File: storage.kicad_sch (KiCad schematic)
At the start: 5 parts, among them J14 DM3CS-SF, U7 MX25V4006EM1I-13G

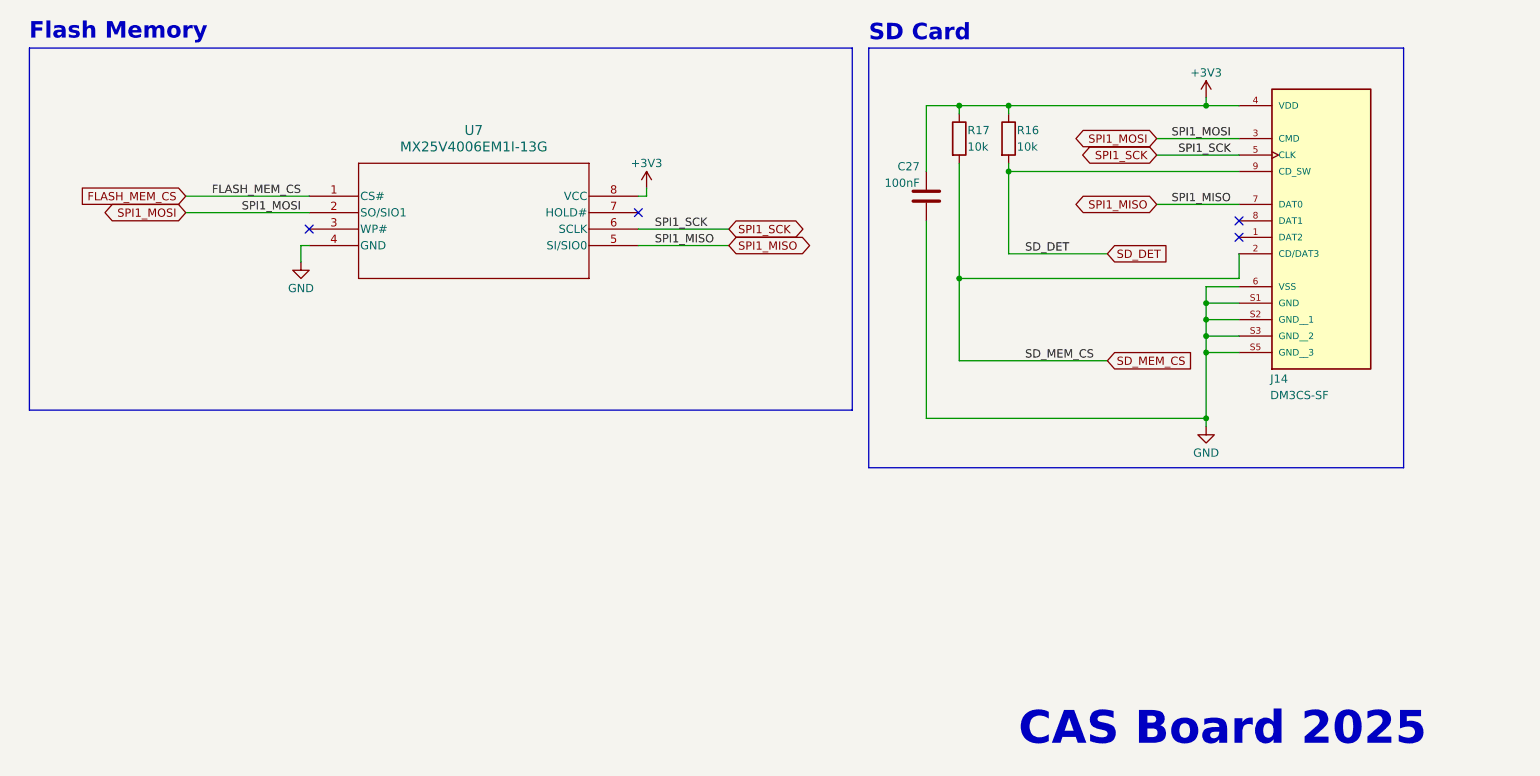
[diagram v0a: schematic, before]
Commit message: Use heirarchical labels
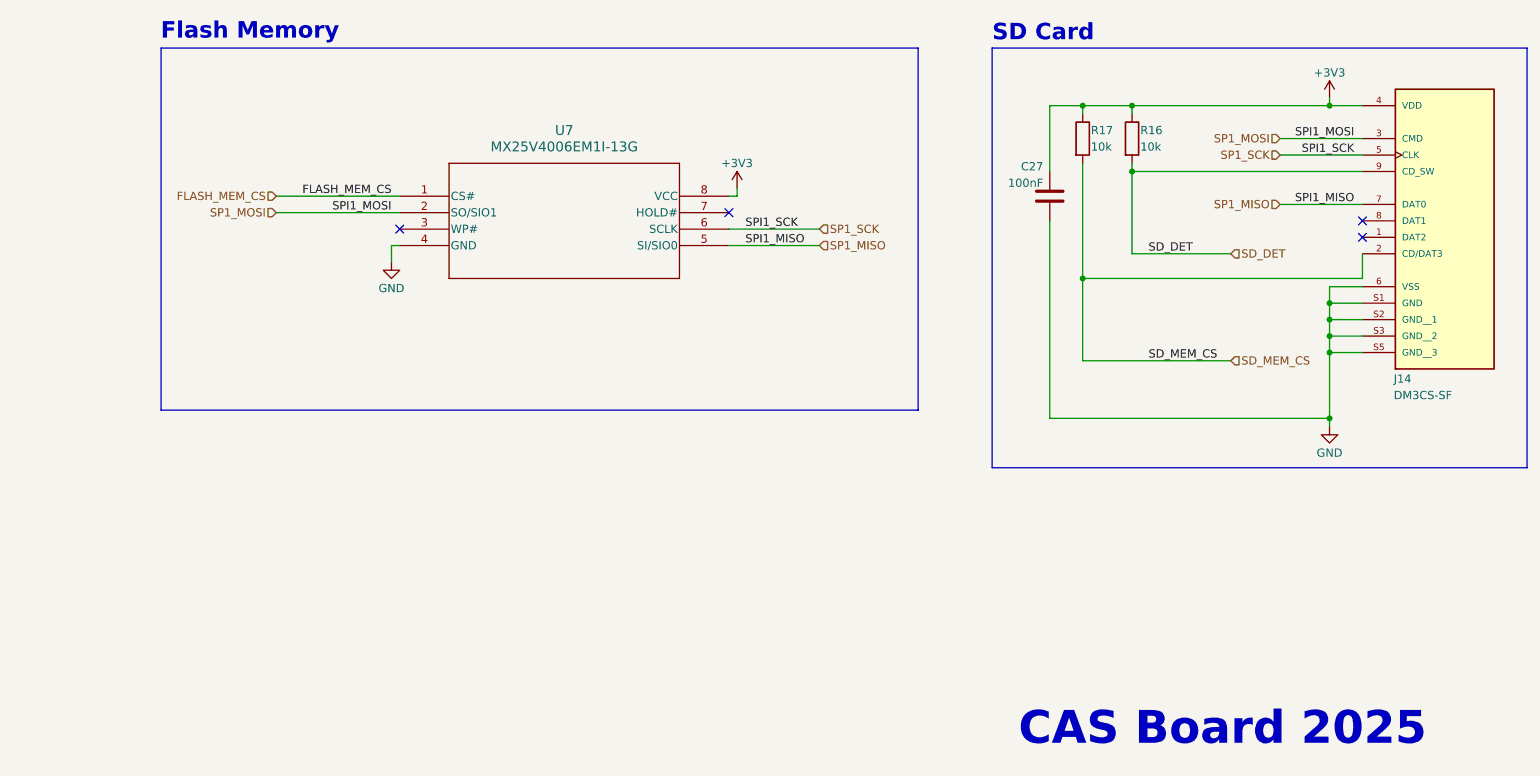
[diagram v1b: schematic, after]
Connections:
- net SPI1_MISO renamed SP1_MISO
- net SPI1_MOSI renamed SP1_MOSI
- net SPI1_SCK renamed SP1_SCK
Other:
- moved on the sheet: C27, J14, R16, R17, U7

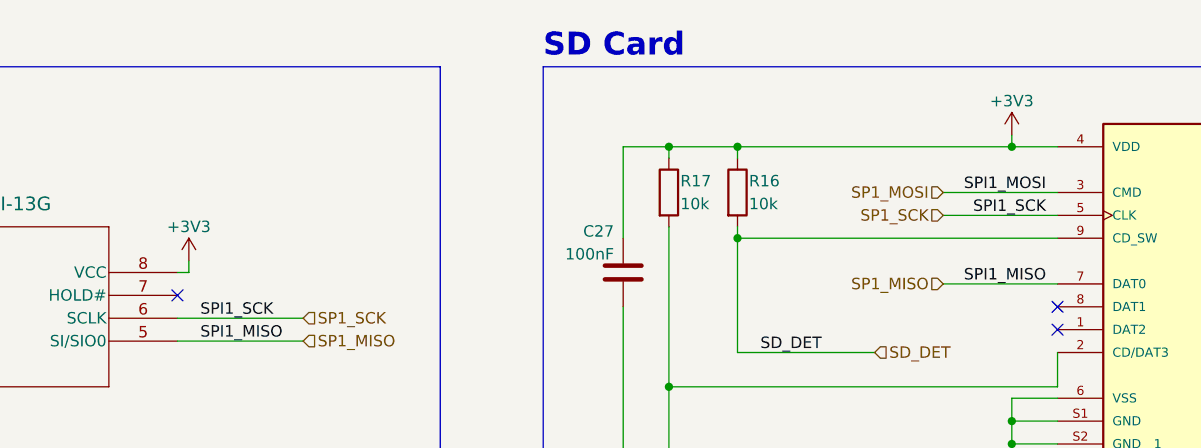
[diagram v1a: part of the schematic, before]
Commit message: Initial layout for PCB components, updated README with images. Removed some test points and headers from final layout. Pending addition of buzzer. Pending additional power testing and pending routing.
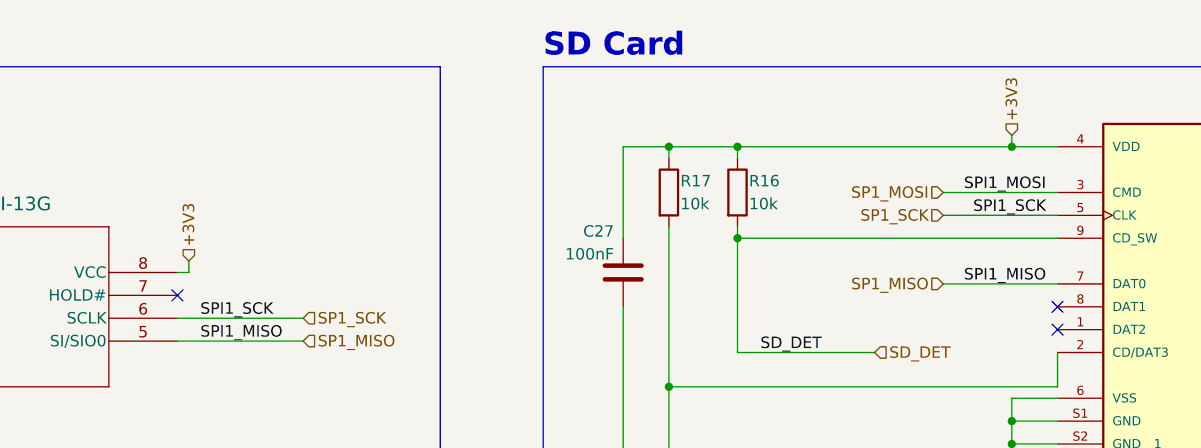
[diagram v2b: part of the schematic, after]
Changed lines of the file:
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@@
+		)
+	)
+	(hierarchical_label "+3V3"
+		(shape input)
+		(at 226.06 76.2 90)
+		(effects
+			(font
+				(size 1.27 1.27)
+			)
+			(justify left)
 		)
 	)
@@
 			)
 			(justify right)
+		)
+	)
+	(hierarchical_label "+3V3"
+		(shape input)
+		(at 134.62 90.17 90)
+		(effects
+			(font
+				(size 1.27 1.27)
+			)
+			(justify left)
 		)
 	)
@@
 	)
 	(symbol
-		(lib_id "power:+3V3")
-		(at 134.62 90.17 0)
-		(unit 1)
-		(exclude_from_sim no)
-		(in_bom yes)
-		(on_board yes)
-		(dnp no)
-		(property "Reference" "#PWR042"
-			(at 134.62 93.98 0)
-			(effects
-				(font
-					(size 1.27 1.27)
-				)
-				(hide yes)
-			)
-		)
-		(property "Value" "+3V3"
-			(at 134.62 86.36 0)
-			(effects
-				(font
-					(size 1.27 1.27)
-				)
-			)
-		)
-		(property "Footprint" ""
-			(at 134.62 90.17 0)
-			(effects
-				(font
-					(size 1.27 1.27)
-				)
-				(hide yes)
-			)
-		)
-		(property "Datasheet" ""
-			(at 134.62 90.17 0)
-			(effects
-				(font
-					(size 1.27 1.27)
-				)
-				(hide yes)
-			)
-		)
-		(property "Description" "Power symbol creates a global label with name \"+3V3\""
-			(at 134.62 90.17 0)
-			(effects
-				(font
-					(size 1.27 1.27)
-				)
-				(hide yes)
-			)
-		)
-		(pin "1"
-		)
-		(instances
-			(project "SimplerFlight_v2"
-				(path "/05521696-5bcb-4d0e-9e87-bbc993e58ce4/5650f10d-f3d9-4005-a2cb-b3a110a98d48"
-					(reference "#PWR042")
-					(unit 1)
-				)
-			)
-		)
-	)
-	(symbol
 		(lib_id "power:GND")
 		(at 81.28 101.6 0)
@@
 					(unit 1)
 				)
-			)
-		)
-	)
-	(symbol
-		(lib_id "power:+3V3")
-		(at 226.06 76.2 0)
-		(unit 1)
-		(exclude_from_sim no)
-		(in_bom yes)
-		(on_board yes)
-		(dnp no)
-		(property "Reference" "#PWR032"
-			(at 226.06 80.01 0)
-			(effects
-				(font
-					(size 1.27 1.27)
-				)
-				(hide yes)
-			)
-		)
-		(property "Value" "+3V3"
-			(at 226.06 72.39 0)
-			(effects
-				(font
-					(size 1.27 1.27)
-				)
-			)
-		)
-		(property "Footprint" ""
-			(at 226.06 76.2 0)
-			(effects
-				(font
-					(size 1.27 1.27)
-				)
-				(hide yes)
-			)
-		)
-		(property "Datasheet" ""
-			(at 226.06 76.2 0)
-			(effects
-				(font
-					(size 1.27 1.27)
-				)
-				(hide yes)
-			)
-		)
-		(property "Description" "Power symbol creates a global label with name \"+3V3\""
-			(at 226.06 76.2 0)
-			(effects
-				(font
-					(size 1.27 1.27)
-				)
-				(hide yes)
-			)
-		)
-		(pin "1"
-		)
-		(instances
-			(project "SimplerFlight_v2"
-				(path "/05521696-5bcb-4d0e-9e87-bbc993e58ce4/5650f10d-f3d9-4005-a2cb-b3a110a98d48"
-					(reference "#PWR032")
-					(unit 1)
-				)

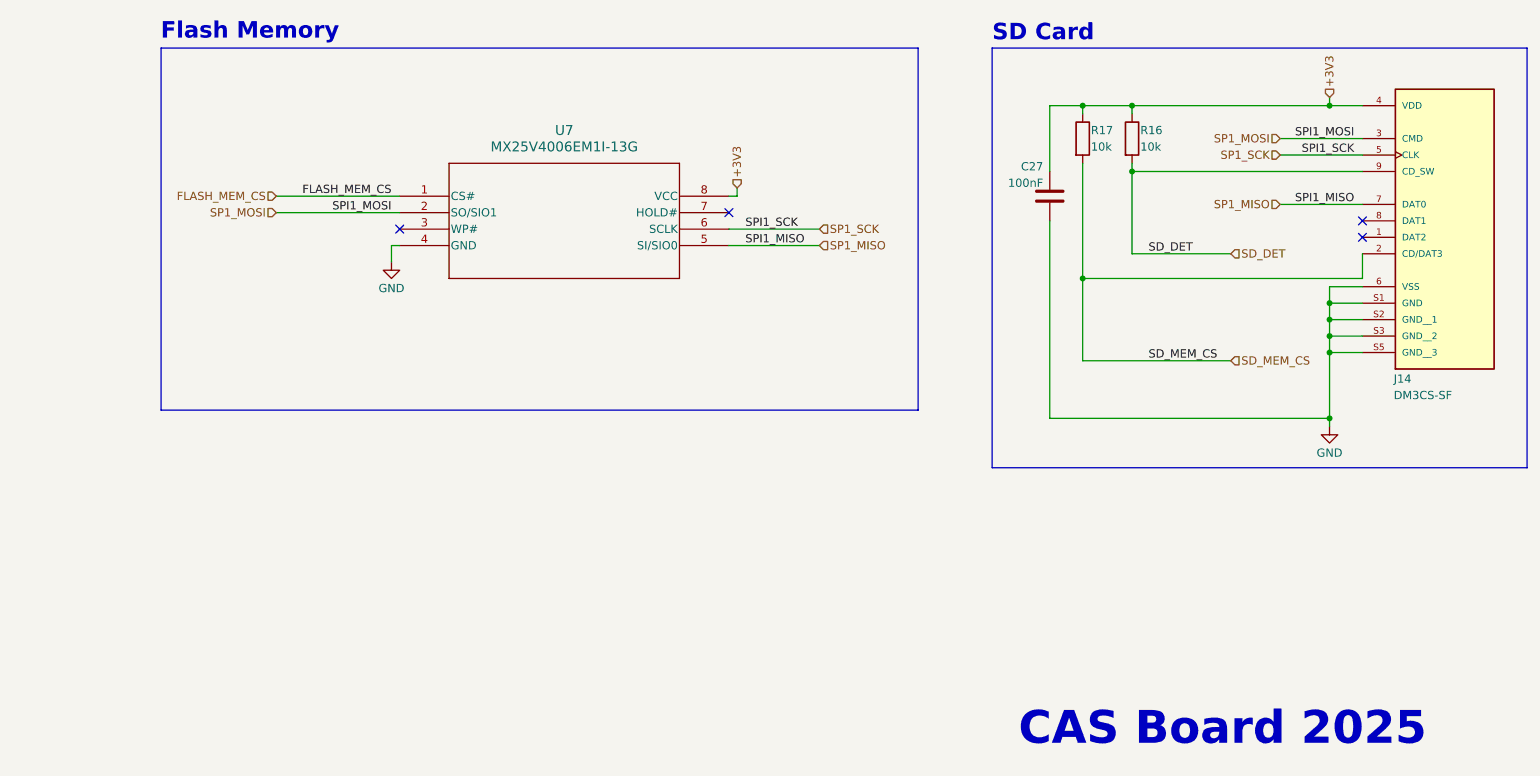
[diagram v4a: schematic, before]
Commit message: Adi made some fixes to schematic
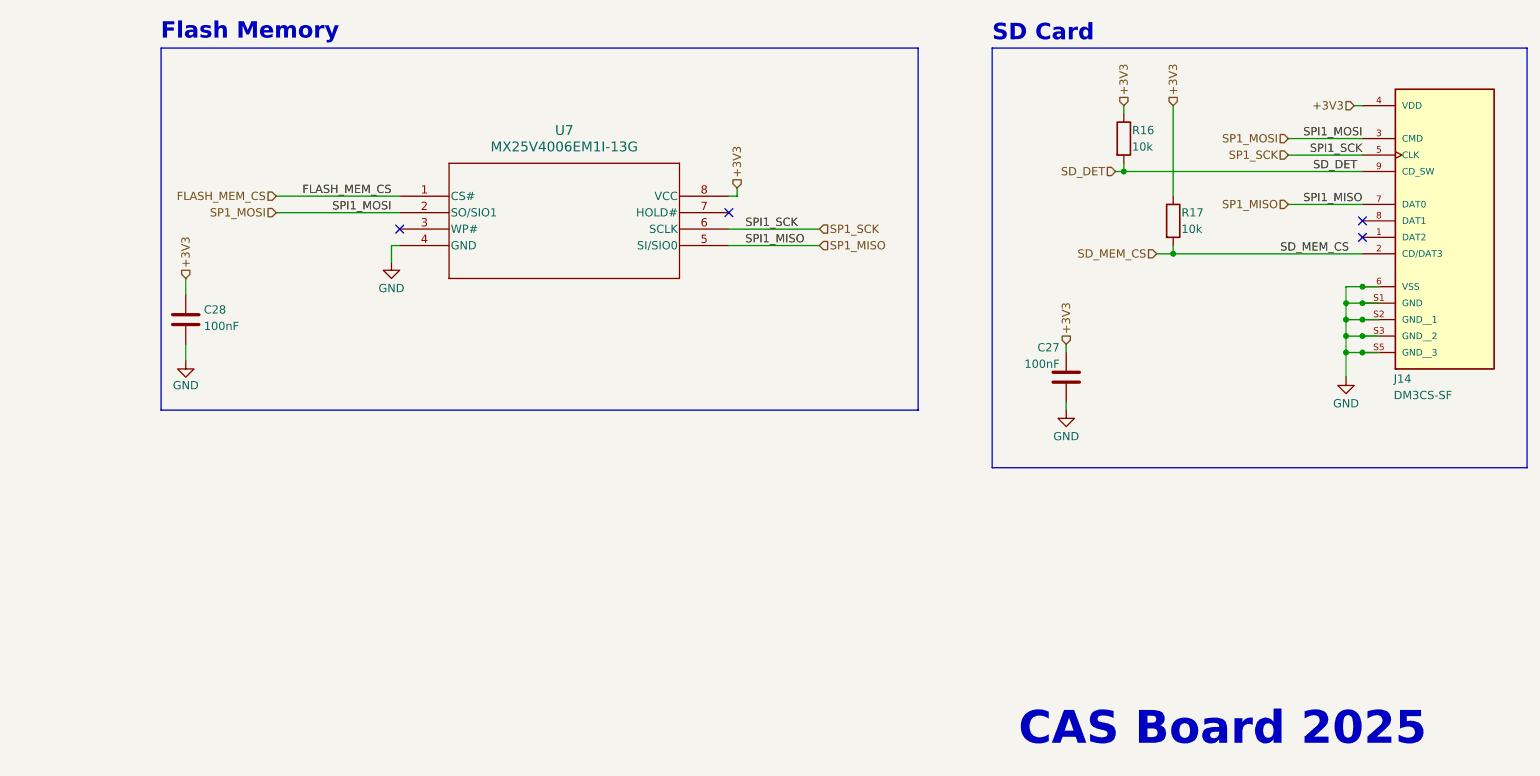
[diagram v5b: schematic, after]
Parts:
- added C28: 100nF, Capacitor_SMD:C_0805_2012Metric, symbol Device:C
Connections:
- net +3V3: now also C28.1
- net GND: now also C28.2
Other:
- moved on the sheet: C27, R16, R17
